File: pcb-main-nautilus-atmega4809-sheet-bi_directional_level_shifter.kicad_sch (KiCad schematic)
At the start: 3 parts, among them Q1 BSS138PW,115

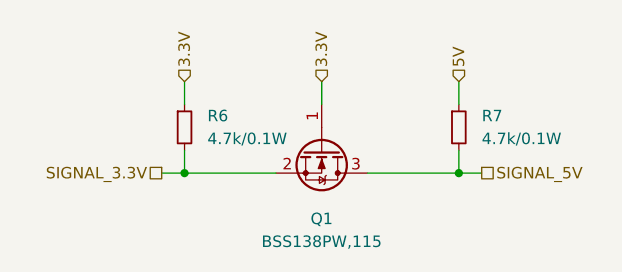
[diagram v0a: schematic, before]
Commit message: Update BOM
Supports #2.
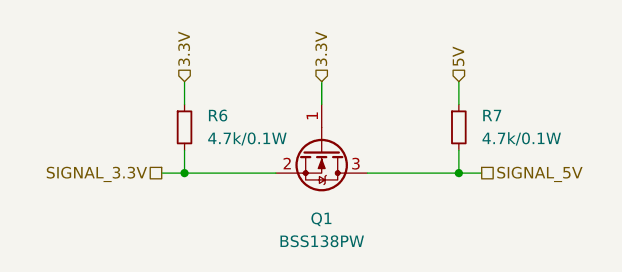
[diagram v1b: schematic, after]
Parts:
- Q1: value BSS138PW,115 -> BSS138PW; Manufacturer Part Number BSS138PW,115 -> BSS138PW
- R6, R7: Manufacturer Part Number ERJ-3EKF4701V -> ERJ-3EKF4701
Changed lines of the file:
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@@
       (effects (font (size 1.27 1.27)) hide)
     )
-    (property "Manufacturer Part Number" "ERJ-3EKF4701V" (id 5) (at 154.94 105.41 0)
+    (property "Manufacturer Part Number" "ERJ-3EKF4701" (id 5) (at 154.94 105.41 0)
       (effects (font (size 1.27 1.27)) hide)
     )
@@
       (effects (font (size 1.27 1.27)) hide)
     )
-    (property "Manufacturer Part Number" "ERJ-3EKF4701V" (id 5) (at 124.46 105.41 0)
+    (property "Manufacturer Part Number" "ERJ-3EKF4701" (id 5) (at 124.46 105.41 0)
       (effects (font (size 1.27 1.27)) hide)
     )
@@
     (in_bom yes) (on_board yes) (fields_autoplaced)
     (property "Reference" "Q1" (id 0) (at 139.7 115.57 90))
-    (property "Value" "BSS138PW,115" (id 1) (at 139.7 118.11 90))
+    (property "Value" "BSS138PW" (id 1) (at 139.7 118.11 90))
     (property "Footprint" "Package_TO_SOT_SMD:SOT-323_SC-70_Handsoldering" (id 2) (at 142.24 113.03 0)
       (effects (font (size 1.27 1.27)) hide)
@@
       (effects (font (size 1.27 1.27)) hide)
     )
-    (property "Manufacturer Part Number" "BSS138PW,115" (id 5) (at 139.7 107.95 90)
+    (property "Manufacturer Part Number" "BSS138PW" (id 5) (at 139.7 107.95 90)
       (effects (font (size 1.27 1.27)) hide)
     )
